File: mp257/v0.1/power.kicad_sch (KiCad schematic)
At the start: 127 parts, among them U1 STM32MP257FAK3, U26 STPMIC25APQR, U9 MCP1501-18xCH

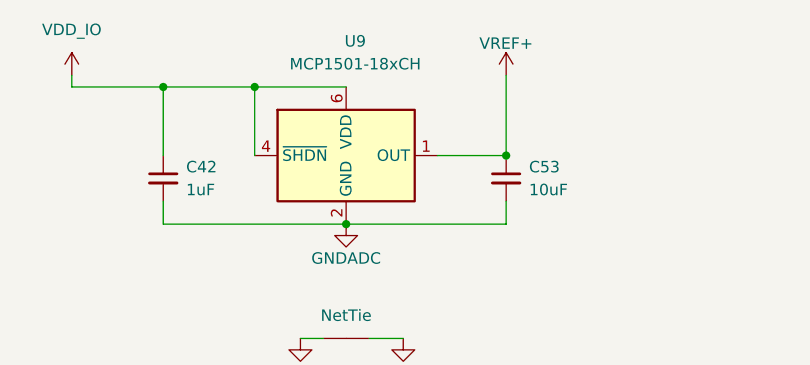
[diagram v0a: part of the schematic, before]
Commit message: Finish board, cleanup BOM
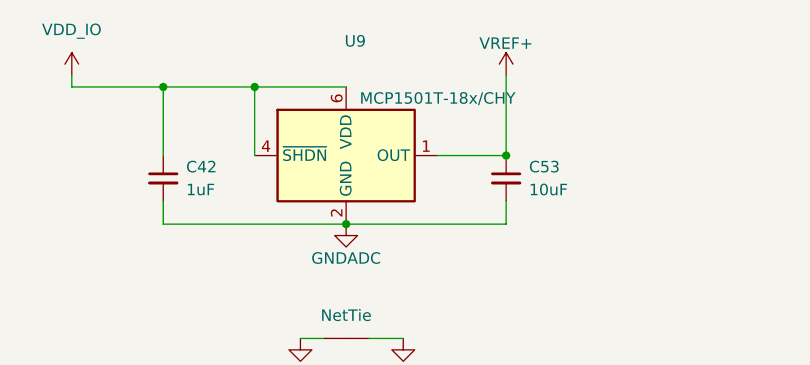
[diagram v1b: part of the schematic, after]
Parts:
- U9: value MCP1501-18xCH -> MCP1501T-18x/CHY; symbol Reference_Voltage:MCP1501-18xCH -> 4ms_Reference:MCP1501T-18E/CHY; JLCPCB ID (none) -> C150807; Manufacturer (none) -> Microchip Tech; Part Number (none) -> MCP1501T-18E/CHY
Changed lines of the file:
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@@
 	)
 	(symbol
-		(lib_id "Reference_Voltage:MCP1501-18xCH")
+		(lib_id "4ms_Reference:MCP1501T-18E/CHY")
 		(at 458.47 48.26 0)
 		(unit 1)
@@
 			)
 		)
-		(property "Value" "MCP1501-18xCH"
-			(at 459.486 38.1 0)
+		(property "Value" "MCP1501T-18x/CHY"
+			(at 468.63 41.91 0)
 			(effects
 				(font
@@
 			)
 		)
-		(property "Datasheet" "http://ww1.microchip.com/downloads/en/DeviceDoc/20005474E.pdf"
+		(property "Datasheet" "https://ww1.microchip.com/downloads/aemDocuments/documents/APID/ProductDocuments/DataSheets/MCP1501-Data-Sheet-DS20005474.pdf"
 			(at 458.47 48.26 0)
 			(effects
@@
 			)
 		)
-		(property "Note" ""
+		(property "Manufacturer" "Microchip Tech"
 			(at 458.47 48.26 0)
 			(effects
+				(font
+					(size 1.27 1.27)
+				)
+				(hide yes)
+			)
+		)
+		(property "Part Number" "MCP1501T-18E/CHY"
+			(at 458.47 48.26 0)
+			(effects
+				(font
+					(size 1.27 1.27)
+				)
+				(hide yes)
+			)
+		)
+		(property "JLCPCB ID" "C150807"
+			(at 458.47 48.26 0)
+			(effects
